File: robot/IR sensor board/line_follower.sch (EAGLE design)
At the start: 8 parts

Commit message: updated schematic and board
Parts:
- JP1: device pinhead:PINHD-1X55X2MM -> pinhead:PINHD-1X5
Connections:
- net N$4: now also JP1.2; no longer JP1.3
- net N$5: now also JP1.3; no longer JP1.2
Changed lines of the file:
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@@
 <?xml version="1.0" encoding="utf-8"?>
 <!DOCTYPE eagle SYSTEM "eagle.dtd">
-<eagle version="7.5.0">
+<eagle version="7.6.0">
 <drawing>
 <settings>
@@
 <part name="P+4" library="supply1" deviceset="VCC" device=""/>
 <part name="R5" library="resistor" deviceset="R-EU_" device="0204/7"/>
-<part name="JP1" library="pinhead" deviceset="PINHD-1X5" device="5X2MM"/>
+<part name="JP1" library="pinhead" deviceset="PINHD-1X5" device=""/>
 <part name="P+5" library="supply1" deviceset="VCC" device=""/>
 <part name="GND5" library="supply1" deviceset="GND" device=""/>
@@
 <wire x1="99.06" y1="76.2" x2="114.3" y2="76.2" width="0.1524" layer="91"/>
 <wire x1="114.3" y1="76.2" x2="114.3" y2="48.26" width="0.1524" layer="91"/>
-<wire x1="114.3" y1="48.26" x2="124.46" y2="48.26" width="0.1524" layer="91"/>
-<wire x1="124.46" y1="48.26" x2="127" y2="45.72" width="0.1524" layer="91"/>
-<pinref part="JP1" gate="A" pin="3"/>
-<wire x1="127" y1="45.72" x2="139.7" y2="45.72" width="0.1524" layer="91"/>
+<pinref part="JP1" gate="A" pin="2"/>
+<wire x1="114.3" y1="48.26" x2="139.7" y2="48.26" width="0.1524" layer="91"/>
 </segment>
 </net>
@@
 <wire x1="86.36" y1="45.72" x2="99.06" y2="45.72" width="0.1524" layer="91"/>
 <wire x1="99.06" y1="45.72" x2="99.06" y2="48.26" width="0.1524" layer="91"/>
-<wire x1="99.06" y1="45.72" x2="124.46" y2="45.72" width="0.1524" layer="91"/>
-<wire x1="124.46" y1="45.72" x2="127" y2="48.26" width="0.1524" layer="91"/>
-<pinref part="JP1" gate="A" pin="2"/>
-<wire x1="127" y1="48.26" x2="139.7" y2="48.26" width="0.1524" layer="91"/>
-</segment>
-</net>
+<wire x1="99.06" y1="45.72" x2="139.7" y2="45.72" width="0.1524" layer="91"/>
+<pinref part="JP1" gate="A" pin="3"/>
+</segment>
+</net>

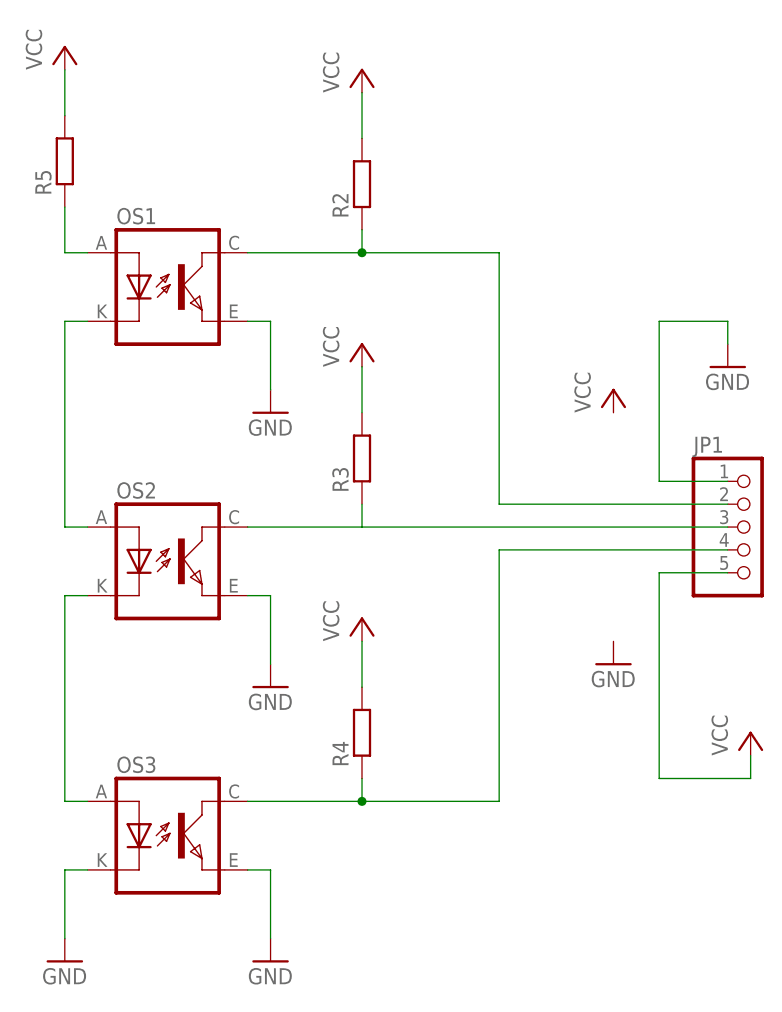
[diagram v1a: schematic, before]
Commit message: updated sensor board
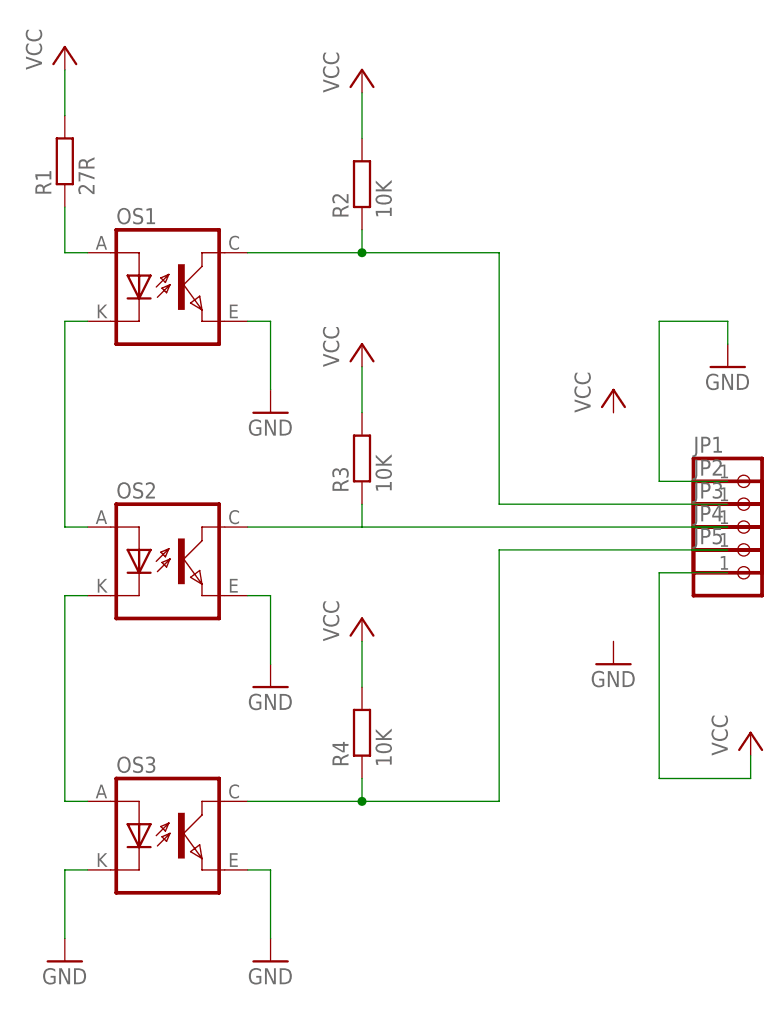
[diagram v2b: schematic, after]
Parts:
- removed R5: (no value), resistor:R-EU_0204/7
- added JP2, JP3, JP4, JP5: (no value), pinhead1:PINHD-1X1
- added R1: 27R, resistor1:R-EU_0204/7
- JP1: device pinhead:PINHD-1X5 -> pinhead1:PINHD-1X1
- R2, R3, R4: value (none) -> 10K; device resistor:R-EU_0204/7 -> resistor1:R-EU_0204/7
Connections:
- net N$3: now also R1.1; no longer R5.1
- net N$4: now also JP2.1; no longer JP1.2
- net N$5: now also JP3.1; no longer JP1.3
- net N$6: now also JP4.1; no longer JP1.4
- net VCC: now also JP5.1, R1.2; no longer JP1.5, R5.2
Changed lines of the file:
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@@
 <part name="GND4" library="supply1" deviceset="GND" device=""/>
 <part name="P+1" library="supply1" deviceset="VCC" device=""/>
-<part name="R2" library="resistor" deviceset="R-EU_" device="0204/7"/>
-<part name="R3" library="resistor" deviceset="R-EU_" device="0204/7"/>
-<part name="R4" library="resistor" deviceset="R-EU_" device="0204/7"/>
+<part name="R2" library="resistor1" deviceset="R-EU_" device="0204/7" value="10K"/>
+<part name="R3" library="resistor1" deviceset="R-EU_" device="0204/7" value="10K"/>
+<part name="R4" library="resistor1" deviceset="R-EU_" device="0204/7" value="10K"/>
 <part name="P+2" library="supply1" deviceset="VCC" device=""/>
 <part name="P+3" library="supply1" deviceset="VCC" device=""/>
 <part name="P+4" library="supply1" deviceset="VCC" device=""/>
-<part name="R5" library="resistor" deviceset="R-EU_" device="0204/7"/>
-<part name="JP1" library="pinhead" deviceset="PINHD-1X5" device=""/>
+<part name="R1" library="resistor1" deviceset="R-EU_" device="0204/7" value="27R"/>
 <part name="P+5" library="supply1" deviceset="VCC" device=""/>
 <part name="GND5" library="supply1" deviceset="GND" device=""/>
 <part name="P+6" library="supply1" deviceset="VCC" device=""/>
 <part name="GND6" library="supply1" deviceset="GND" device=""/>
+<part name="JP1" library="pinhead1" deviceset="PINHD-1X1" device=""/>
+<part name="JP2" library="pinhead1" deviceset="PINHD-1X1" device=""/>
+<part name="JP3" library="pinhead1" deviceset="PINHD-1X1" device=""/>
+<part name="JP4" library="pinhead1" deviceset="PINHD-1X1" device=""/>
+<part name="JP5" library="pinhead1" deviceset="PINHD-1X1" device=""/>
 </parts>
 <sheets>
@@
 <instance part="P+3" gate="VCC" x="99.06" y="66.04"/>
 <instance part="P+4" gate="VCC" x="99.06" y="35.56"/>
-<instance part="R5" gate="G$1" x="66.04" y="86.36" rot="R90"/>
-<instance part="JP1" gate="A" x="142.24" y="45.72"/>
+<instance part="R1" gate="G$1" x="66.04" y="86.36" rot="R90"/>
 <instance part="P+5" gate="VCC" x="127" y="60.96"/>
 <instance part="GND5" gate="1" x="127" y="30.48"/>
 <instance part="P+6" gate="VCC" x="142.24" y="22.86"/>
 <instance part="GND6" gate="1" x="139.7" y="63.5"/>
+<instance part="JP1" gate="G$1" x="142.24" y="50.8"/>
+<instance part="JP2" gate="G$1" x="142.24" y="48.26"/>
+<instance part="JP3" gate="G$1" x="142.24" y="45.72"/>
+<instance part="JP4" gate="G$1" x="142.24" y="43.18"/>
+<instance part="JP5" gate="G$1" x="142.24" y="40.64"/>
 </instances>
 <busses>
@@
 </segment>
 <segment>
-<pinref part="JP1" gate="A" pin="1"/>
 <wire x1="139.7" y1="50.8" x2="132.08" y2="50.8" width="0.1524" layer="91"/>
 <wire x1="132.08" y1="50.8" x2="132.08" y2="68.58" width="0.1524" layer="91"/>
@@
 <wire x1="132.08" y1="68.58" x2="139.7" y2="68.58" width="0.1524" layer="91"/>
 <wire x1="139.7" y1="68.58" x2="139.7" y2="66.04" width="0.1524" layer="91"/>
+<pinref part="JP1" gate="G$1" pin="1"/>
 </segment>
 </net>
 <net name="N$3" class="0">
 <segment>
-<pinref part="R5" gate="G$1" pin="1"/>
+<pinref part="R1" gate="G$1" pin="1"/>
 <pinref part="OS1" gate="OS" pin="ANODE"/>
 <wire x1="66.04" y1="81.28" x2="66.04" y2="76.2" width="0.1524" layer="91"/>
@@
 <segment>
 <pinref part="P+1" gate="VCC" pin="VCC"/>
-<pinref part="R5" gate="G$1" pin="2"/>
+<pinref part="R1" gate="G$1" pin="2"/>
 <wire x1="66.04" y1="96.52" x2="66.04" y2="91.44" width="0.1524" layer="91"/>
 </segment>
@@
 </segment>
 <segment>
-<pinref part="JP1" gate="A" pin="5"/>
 <wire x1="139.7" y1="40.64" x2="132.08" y2="40.64" width="0.1524" layer="91"/>
 <wire x1="132.08" y1="40.64" x2="132.08" y2="17.78" width="0.1524" layer="91"/>
@@
 <wire x1="132.08" y1="17.78" x2="142.24" y2="17.78" width="0.1524" layer="91"/>
 <wire x1="142.24" y1="17.78" x2="142.24" y2="20.32" width="0.1524" layer="91"/>
+<pinref part="JP5" gate="G$1" pin="1"/>
 </segment>
 </net>
@@
 <wire x1="99.06" y1="76.2" x2="114.3" y2="76.2" width="0.1524" layer="91"/>
 <wire x1="114.3" y1="76.2" x2="114.3" y2="48.26" width="0.1524" layer="91"/>
-<pinref part="JP1" gate="A" pin="2"/>
 <wire x1="114.3" y1="48.26" x2="139.7" y2="48.26" width="0.1524" layer="91"/>
+<pinref part="JP2" gate="G$1" pin="1"/>
 </segment>
 </net>
@@
 <wire x1="99.06" y1="45.72" x2="99.06" y2="48.26" width="0.1524" layer="91"/>
 <wire x1="99.06" y1="45.72" x2="139.7" y2="45.72" width="0.1524" layer="91"/>
-<pinref part="JP1" gate="A" pin="3"/>
+<pinref part="JP3" gate="G$1" pin="1"/>
 </segment>
 </net>
@@
 <wire x1="99.06" y1="15.24" x2="114.3" y2="15.24" width="0.1524" layer="91"/>
 <wire x1="114.3" y1="15.24" x2="114.3" y2="43.18" width="0.1524" layer="91"/>
-<pinref part="JP1" gate="A" pin="4"/>
 <wire x1="114.3" y1="43.18" x2="139.7" y2="43.18" width="0.1524" layer="91"/>
+<pinref part="JP4" gate="G$1" pin="1"/>
 </segment>
 </net>
